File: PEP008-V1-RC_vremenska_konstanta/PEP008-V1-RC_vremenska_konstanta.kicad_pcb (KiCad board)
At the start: 2 copper layers, 45 x 45 mm, 20 parts, among them J1 Conn_01x01_Pin, J2 Screw_Terminal_01x02, J3 Conn_01x01_Pin, J4 Conn_01x01_Pin, SW1 SW_SPDT, SW2 SW_SPDT

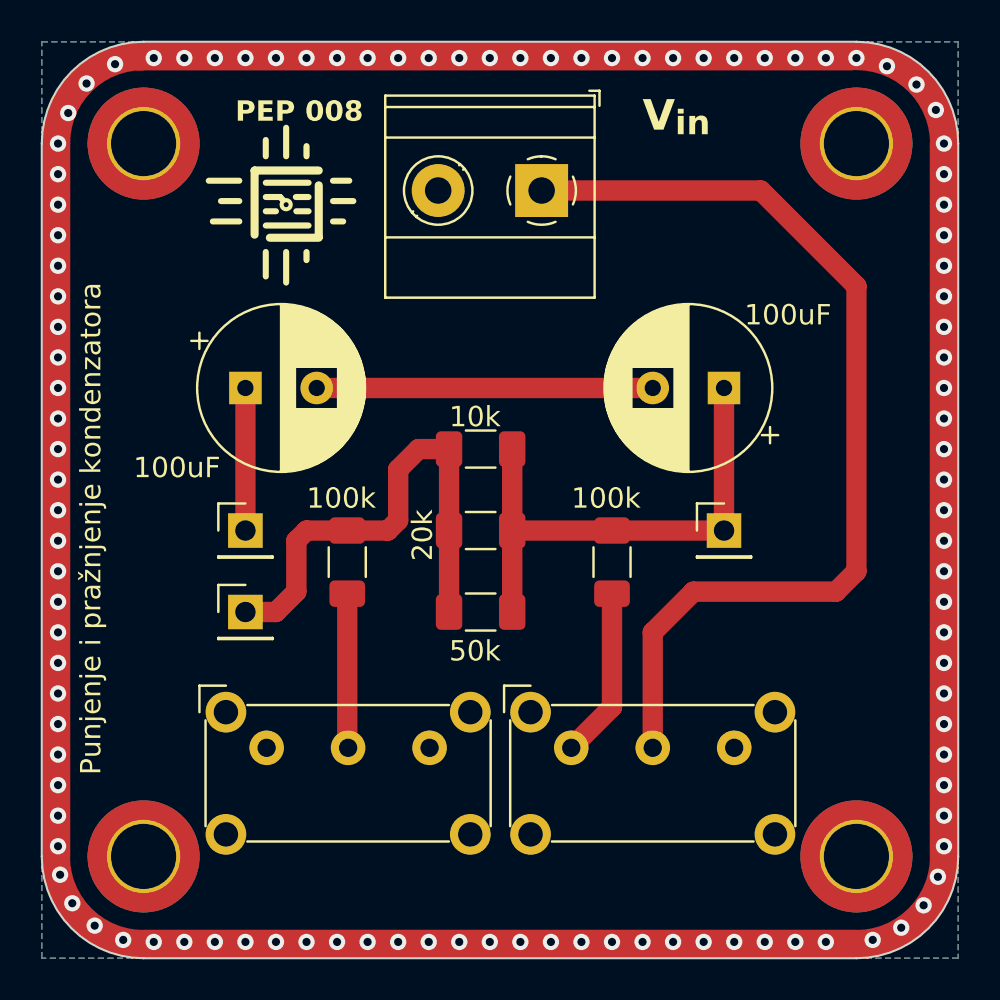
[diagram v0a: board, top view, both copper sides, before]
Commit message: PEP006 and PEP009 update.
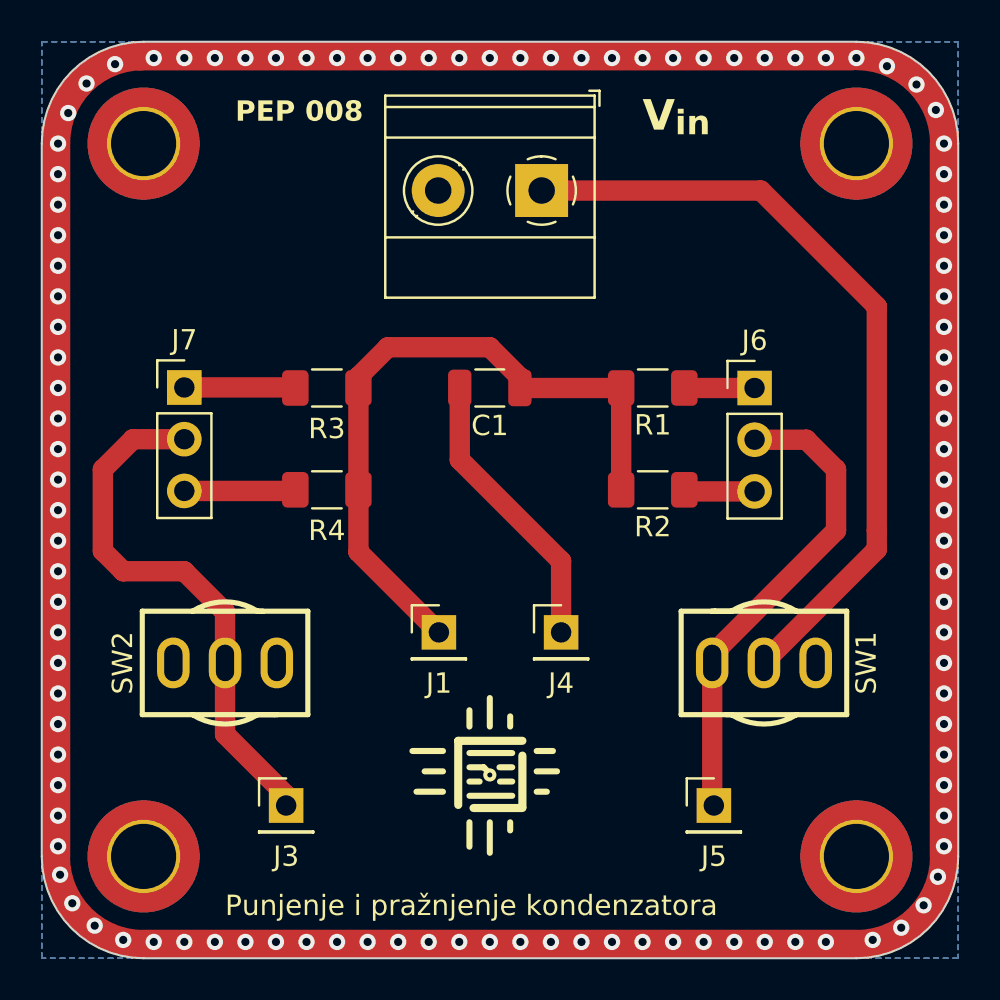
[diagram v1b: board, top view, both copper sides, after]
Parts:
- removed C2: 100u, Capacitor_THT:CP_Radial_D8.0mm_P3.50mm
- removed R5: 50k, Resistor_SMD:R_1206_3216Metric_Pad1.30x1.75mm_HandSolder
- removed the REF** at (135.5, 73.5)
- removed the REF** at (115.5, 73.5)
- added J5: Conn_01x01_Pin, Connector_PinHeader_2.54mm:PinHeader_1x01_P2.54mm_Vertical, F.Cu at (137.0, 98.5)
- added J6: Conn_01x03_Pin, Connector_PinHeader_2.54mm:PinHeader_1x03_P2.54mm_Vertical, F.Cu at (139.0, 78.0)
- added J7: Conn_01x03_Pin, Connector_PinHeader_2.54mm:PinHeader_1x03_P2.54mm_Vertical, F.Cu at (111.0, 78.0)
- C1: value 100u -> 47u; footprint Capacitor_THT:CP_Radial_D8.0mm_P3.50mm -> Capacitor_SMD:C_1206_3216Metric
- R2: value 100k -> 47k
- R3: value 10k -> 100k
- R4: value 20k -> 47k
- SW1, SW2: footprint Button_Switch_THT:SW_E-Switch_EG1224_SPDT_Angled -> PEP_library:SW-TH_2MS1T1B1M1QES-5
- moved REF** 29.7 mm to (126.0, 97.0)
- moved J4 16.3 mm to (129.5, 90.0)
- moved R2 15.4 mm to (134.0, 83.0), turned to 180 degrees
- moved J1 14.9 mm to (123.5, 90.0)
- moved C1 11.5 mm to (126.0, 78.0)
- moved SW1 10.3 mm to (139.5, 91.5), turned to -90 degrees
- moved J3 9.71 mm to (116.0, 98.5)
- moved R1 8.78 mm to (134.0, 78.0), turned to 180 degrees
- moved R3 8.12 mm to (118.0, 78.0)
- moved R4 7.81 mm to (118.0, 83.0)
- moved SW2 4.64 mm to (113.0, 91.5), turned to 90 degrees
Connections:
- C1 pad 2: Net-(C1-Pad2) -> 0
- R1 pad 1: Net-(SW1-A) -> Net-(J6-Pin_1)
- R2 pad 1: Net-(SW2-B) -> Net-(J6-Pin_3)
- R2 pad 2: Net-(J3-Pin_1) -> Output voltage
- R3 pad 1: Net-(J3-Pin_1) -> Net-(J7-Pin_1)
- R4 pad 1: Net-(J3-Pin_1) -> Net-(J7-Pin_3)
- SW1 pad 1: Net-(SW1-A) -> Net-(J5-Pin_1)
- SW2 pad 2: Net-(SW2-B) -> Net-(J3-Pin_1)
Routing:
- net Net-(J5-Pin_1): track 0.00 -> 23.7 mm
- net Net-(C1-Pad2): track 16.7 -> 0.00 mm
- net Input voltage: track 48.3 -> 38.6 mm
- net Net-(SW1-A): track 8.40 -> 0.00 mm
- net Output voltage: track 25.6 -> 33.8 mm
- net Net-(SW2-B): track 7.59 -> 0.00 mm
- net 0: track 7.00 -> 14.1 mm
- net Net-(J7-Pin_3): track 0.00 -> 5.47 mm
- net Net-(J7-Pin_1): track 0.00 -> 5.46 mm
- net Net-(J6-Pin_3): track 0.00 -> 3.48 mm
- net Net-(J6-Pin_1): track 0.00 -> 3.45 mm
- net Net-(J3-Pin_1): track 24.2 -> 26.6 mm
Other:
- board text removed: "100k"
- board text removed: "100uF"
- board text removed: "10k"
- board text removed: "20k"
- board text removed: "50k"
